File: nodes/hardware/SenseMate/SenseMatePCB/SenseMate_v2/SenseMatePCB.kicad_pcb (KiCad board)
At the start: 2 copper layers, 38.7 x 61.8 mm, 16 parts, among them J1 Conn_01x04, J2 Conn_02x06_Counter_Clockwise 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, M1 Motor_DC, Q1 2SC1815, Q2 2SC1815, SW5 SW_DPDT_x2, U1 XIAO-nRF52840-Plus-SMD, U2 RFM95W-868S2

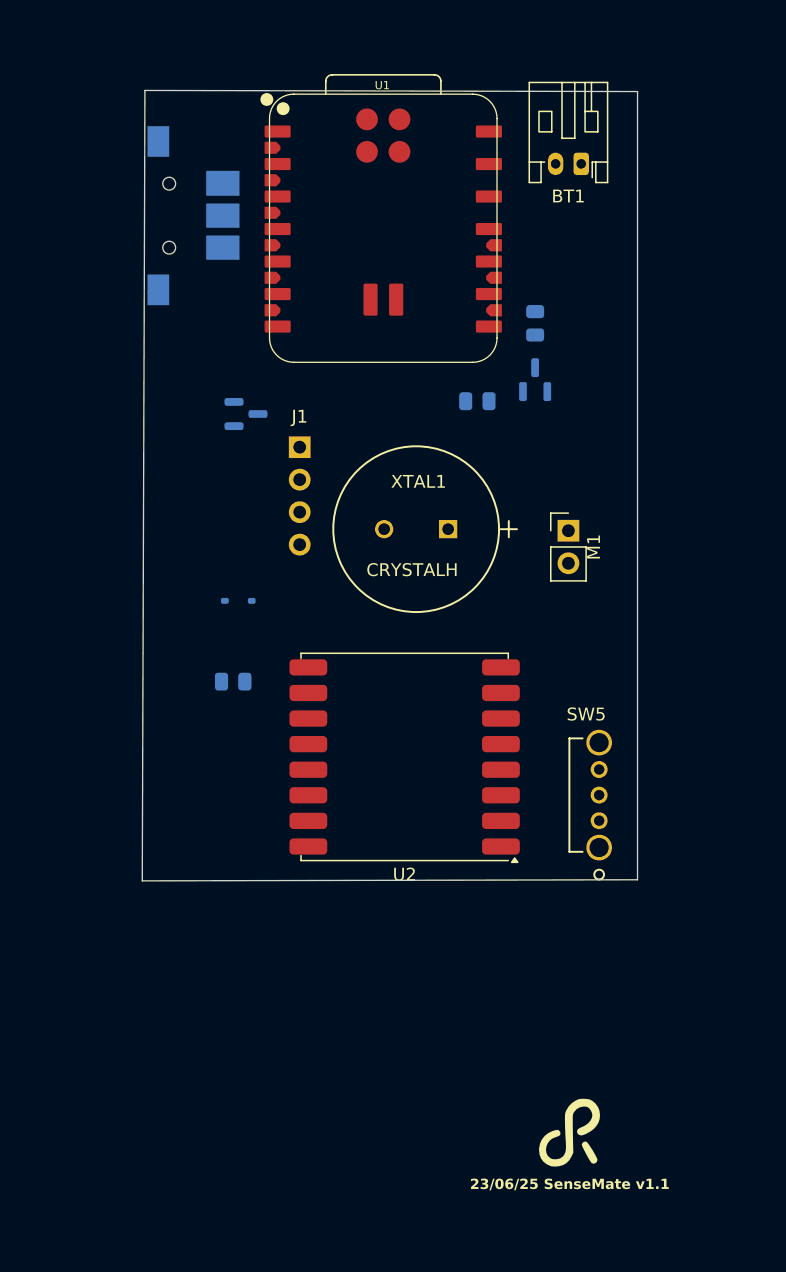
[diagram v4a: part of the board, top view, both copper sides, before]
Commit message: added wireing and copperboard
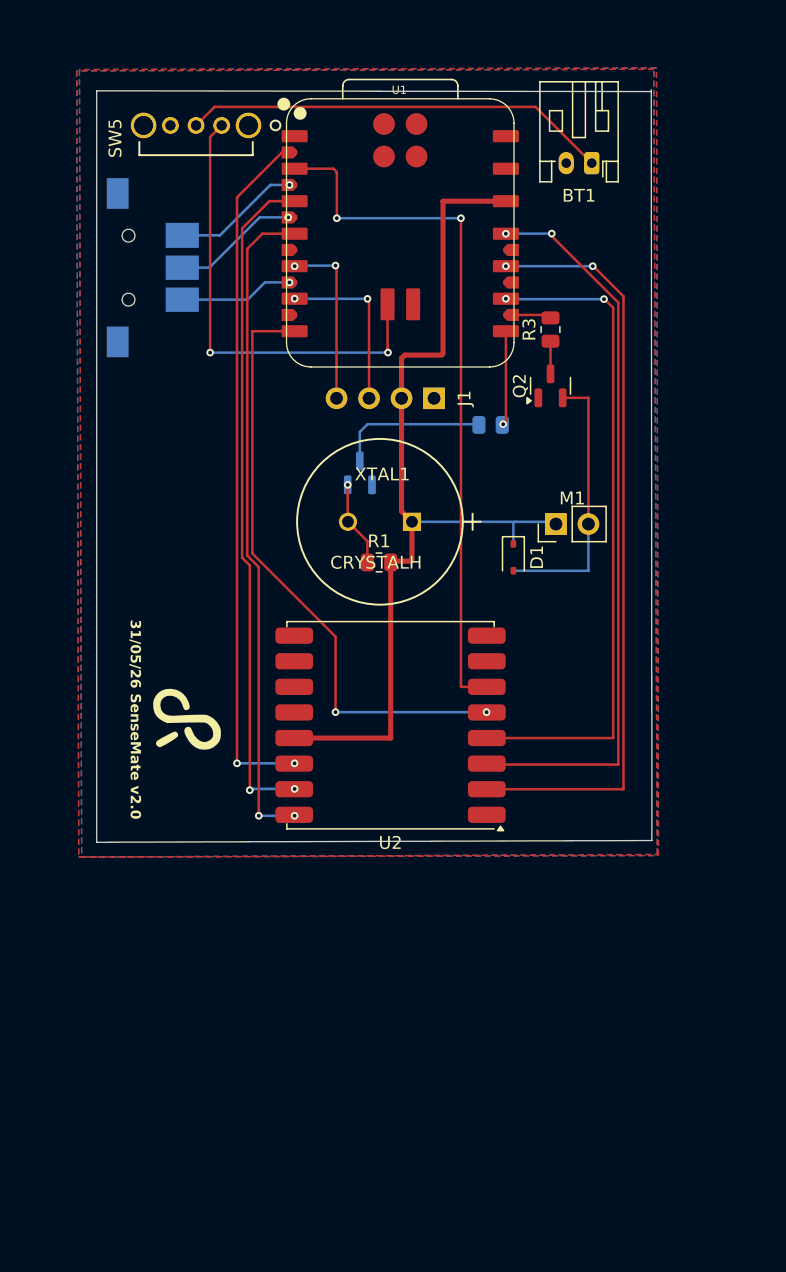
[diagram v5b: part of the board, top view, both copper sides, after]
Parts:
- D1, Q2, R1, R3: moved to F.Cu
- moved SW5 61.8 mm to (88.1, 30.8), turned to 180 degrees
- moved G*** 44.0 mm to (85.4, 79.8), turned to -90 degrees
- moved D1 21.8 mm to (110.9, 64.6), turned to -90 degrees
- moved R1 14.7 mm to (100.4, 65.0), turned to 0 degrees
- moved J1 11.2 mm to (104.7, 52.2), turned to 90 degrees
- moved Q1 10.0 mm to (98.9, 58.0), turned to 90 degrees
- moved S1 5.16 mm to (80.8, 42.0)
- moved XTAL1 2.89 mm to (103.0, 61.8)
- moved U2 2.71 mm to (101.3, 77.7)
- moved R2 2.12 mm to (109.1, 54.3)
- moved U1 1.38 mm to (102.1, 39.3)
- moved Q2 1.30 mm to (113.8, 51.2)
- moved R3 1.30 mm to (113.8, 46.8)
- moved M1 1.11 mm to (114.2, 62.0), turned to 90 degrees
- moved BT1 0.83 mm to (117.0, 33.8)
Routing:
- net +3V3: track 0.00 -> 72.4 mm
- net LoRa_MISO: track 0.00 -> 59.4 mm, vias 0 -> 2
- net LoRa_MOSI: track 0.00 -> 57.6 mm, vias 0 -> 2
- net LoRa_RST: track 0.00 -> 55.3 mm, vias 0 -> 2
- net LoRa_DIO0: track 0.00 -> 54.3 mm, vias 0 -> 2
- net LoRa_DIO1: track 0.00 -> 52.7 mm, vias 0 -> 2
- net LoRa_SCK: track 0.00 -> 52.2 mm, vias 0 -> 2
- net LoRa_DIO2: track 0.00 -> 51.8 mm, vias 0 -> 2
- net LoRa_NSS: track 0.00 -> 47.6 mm, vias 0 -> 2
- net VBAT: track 0.00 -> 35.8 mm, vias 0 -> 2
- net Net-(BT1-+): track 0.00 -> 33.3 mm
- net Net-(D1-A): track 0.00 -> 21.4 mm
- net SDA: track 0.00 -> 13.6 mm, vias 0 -> 2
- net SCL: track 0.00 -> 13.5 mm, vias 0 -> 2
- net Net-(Q1-B): track 0.00 -> 11.8 mm
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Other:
- board size 38.7 x 61.8 mm -> 43.4 x 58.8 mm
- board text added: "31/05/26 SenseMate v2.0"
- board text removed: "23/06/25 SenseMate v1.1"

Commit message: fixed Errors
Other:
- board size 43.4 x 58.8 mm -> 43.4 x 60 mm
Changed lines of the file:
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@@
 	(gr_line
 		(start 78.3336 86.868)
-		(end 78.3336 28.144857)
+		(end 78.3336 26.916584)
 		(stroke
 			(width 0.058206)
@@
 	)
 	(gr_line
-		(start 121.675115 28.201403)
-		(end 78.3336 28.144857)
+		(start 121.675057 26.97313)
+		(end 78.333542 26.916584)
 		(stroke
 			(width 0.070379)
@@
 	(gr_line
 		(start 121.725 86.734)
-		(end 121.675 28.066)
+		(end 121.674069 26.973129)
 		(stroke
 			(width 0.070379)

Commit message: redesign parts wip V2.1
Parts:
- BT1: moved to B.Cu
- J1, Q1, R2, S1: moved to F.Cu
- moved M1 33.7 mm to (82.0, 52.0)
- moved Q2 31.7 mm to (82.4, 46.5), turned to 0 degrees
- moved J1 31.6 mm to (111.5, 83.0), turned to -90 degrees
- moved R3 26.8 mm to (87.0, 46.0)
- moved S1 22.5 mm to (81.5, 64.5), turned to 90 degrees
- moved XTAL1 21.8 mm to (89.0, 78.5)
- moved U2 19.9 mm to (108.0, 59.0)
- moved R2 19.6 mm to (91.5, 62.9), turned to 90 degrees
- moved Q1 12.4 mm to (91.5, 67.9)
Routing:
- net GND: track 0.00 -> 2.02 mm
- net Net-(D1-A): track 21.4 -> 19.4 mm

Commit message: pcb version 2.1 done
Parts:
- added J3: Conn_Coaxial, Connector_Coaxial:U.FL_Molex_MCRF_73412-0110_Vertical, F.Cu at (95.9, 55.5)
- moved G*** 40.7 mm to (84.3, 39.2)
- moved D1 29.1 mm to (83.4, 54.9), turned to 0 degrees
- moved R2 26.3 mm to (113.3, 48.3)
- moved R1 10.9 mm to (91.4, 71.1), turned to -90 degrees
- moved R3 1.71 mm to (86.0, 47.4), turned to -90 degrees
- moved Q1 1.34 mm to (90.5, 67.0)
- moved M1 0.99 mm to (82.3, 51.1)
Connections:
- U1 pad 21: VIB_EN -> LoRa_NSS
- U1 pad 7: LoRa_NSS -> VIB_EN
- U2 pad 9: unconnected-(U2-ANT-Pad9) -> Net-(J3-Ext)
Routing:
- net SCL: track 13.5 -> 53.3 mm
- net SDA: track 13.6 -> 53.0 mm
- net +3V3: track 72.4 -> 104.7 mm, vias 0 -> 3
- net Net-(Q1-B): track 11.8 -> 43.0 mm, vias 0 -> 2
- net TMB1: track 10.0 -> 39.6 mm, vias 1 -> 2
- net LoRa_MISO: track 59.4 -> 30.5 mm
- net LoRa_SCK: track 52.2 -> 23.5 mm, vias 2 -> 0
- net LoRa_MOSI: track 57.6 -> 29.2 mm, vias 2 -> 0
- net LoRa_NSS: track 47.6 -> 19.3 mm, vias 2 -> 0
- net TMBT1: track 9.90 -> 34.1 mm, vias 1 -> 2
- net TMB2: track 8.93 -> 26.7 mm, vias 1 -> 2
- net LoRa_RST: track 55.3 -> 38.9 mm
- net LoRa_DIO2: track 51.8 -> 38.1 mm
- net LoRa_DIO1: track 52.7 -> 40.6 mm
- net LoRa_DIO0: track 54.3 -> 43.0 mm
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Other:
- board text added: "31/05/26 SenseMate v2.1"
- board text removed: "31/05/26 SenseMate v2.0"
